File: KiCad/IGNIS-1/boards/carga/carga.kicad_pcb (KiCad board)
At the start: 2 copper layers, 62 x 62 mm, 12 parts, among them J1 LiPo_1S, J2 RBF_pin, J40 Backplane, SW1 Main_SW, U2 TPS63020, U40 TP4056

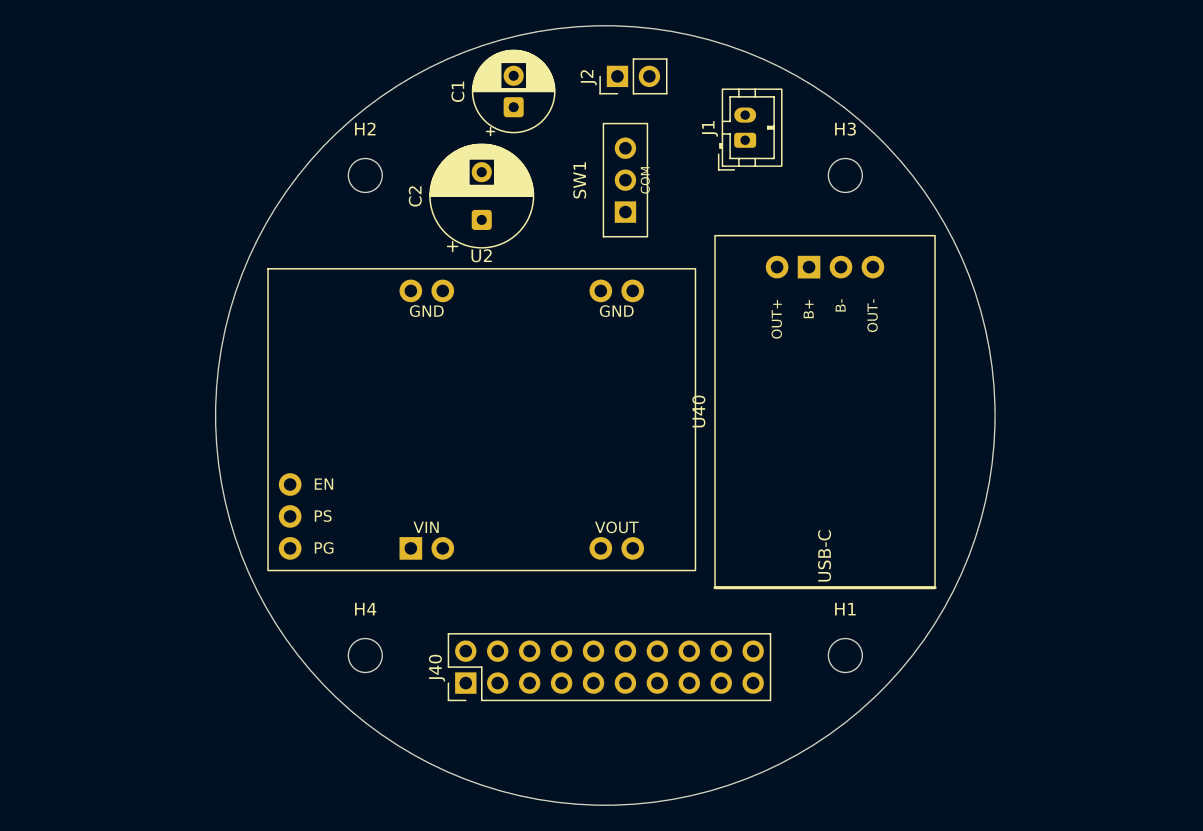
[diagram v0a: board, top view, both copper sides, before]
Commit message: wip: recableo backplane split en progreso (GUI) + doc con move TPS63020
Co-Authored-By: Claude Opus 4.8 <noreply@anthropic.com>
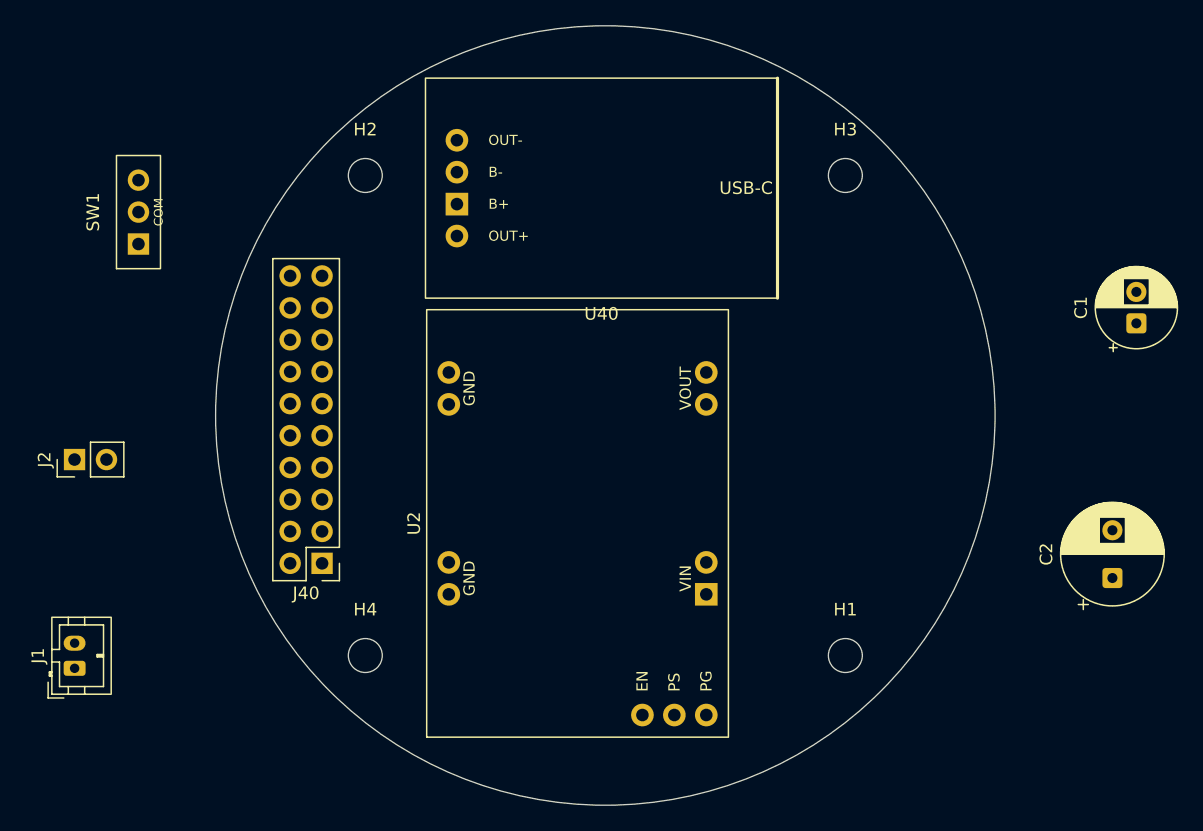
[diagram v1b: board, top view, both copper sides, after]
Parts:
- moved J1 67.9 mm to (57.8, 120.1)
- moved C2 57.7 mm to (140.3, 112.9)
- moved J2 52.9 mm to (57.8, 103.5)
- moved C1 52.4 mm to (142.2, 92.7)
- moved SW1 38.8 mm to (62.9, 83.8)
- moved U40 25.1 mm to (99.7, 81.9), turned to 180 degrees
- moved J40 14.9 mm to (77.5, 111.8), turned to 180 degrees
- moved U2 11.2 mm to (97.8, 108.6), turned to 90 degrees
